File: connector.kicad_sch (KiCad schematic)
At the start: 4 parts, among them J1 Screw_Terminal_01x04

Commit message: ongoing add of MCU, etc.
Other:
- title: multiplex I2C to 6P4C connectors -> Multiplex I2C to Screw Terminal connectors
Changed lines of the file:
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@@
 	(paper "A4")
 	(title_block
-		(title "multiplex I2C to 6P4C connectors")
-		(date "2024-07-25")
-		(rev "v0.1.0")
+		(title "Multiplex I2C to Screw Terminal connectors")
+		(date "2025-09-07")
+		(rev "v0.2.0")
 	)
 	(junction

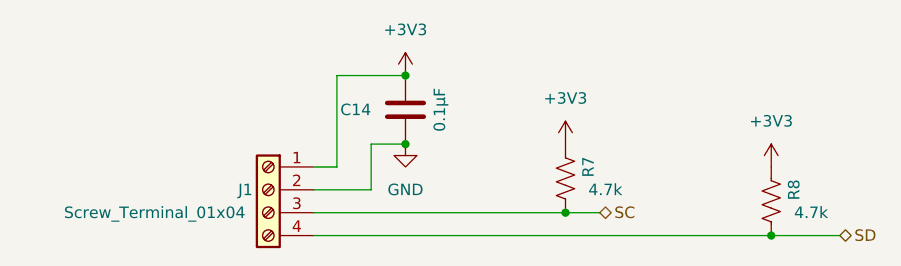
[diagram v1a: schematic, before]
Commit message: symbols an footprints added for f411 change. ERC passes.
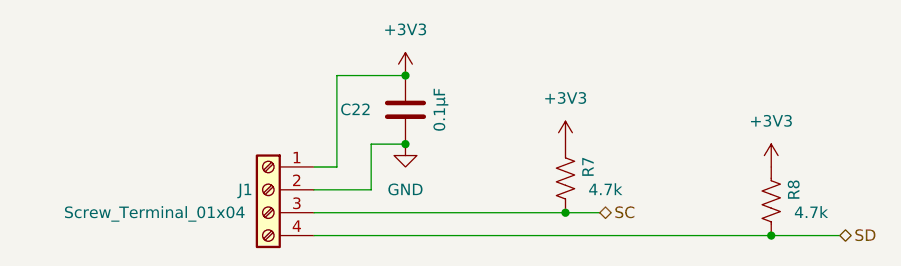
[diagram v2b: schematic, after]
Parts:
- renumbered C14 to C22
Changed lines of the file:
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@@
 			(project "multiplexI2CwithRJ11"
 				(path "/0c2d0c14-8850-4a30-bb78-b2f40cb442ba/0e7b750d-8e4e-450e-948f-cf92910adbb7"
-					(reference "#PWR051")
+					(reference "#PWR016")
 					(unit 1)
 				)
 				(path "/0c2d0c14-8850-4a30-bb78-b2f40cb442ba/24b4e8ef-9825-49f5-9404-579a6ea7b19b"
-					(reference "#PWR059")
+					(reference "#PWR025")
 					(unit 1)
 				)
 				(path "/0c2d0c14-8850-4a30-bb78-b2f40cb442ba/28f5dbbe-14b4-4c25-86a6-457951a84750"
-					(reference "#PWR071")
+					(reference "#PWR040")
 					(unit 1)
 				)
 				(path "/0c2d0c14-8850-4a30-bb78-b2f40cb442ba/4d3cd71d-38ce-404a-8590-119e12741a1e"
-					(reference "#PWR055")
+					(reference "#PWR021")
 					(unit 1)
 				)
 				(path "/0c2d0c14-8850-4a30-bb78-b2f40cb442ba/8a12c970-6e82-4f99-ab8e-e5d673f5e8d9"
-					(reference "#PWR045")
+					(reference "#PWR012")
 					(unit 1)
 				)
 				(path "/0c2d0c14-8850-4a30-bb78-b2f40cb442ba/96274ab6-b7f5-49e6-b2bc-a2b6a3cb42d1"
-					(reference "#PWR067")
+					(reference "#PWR033")
 					(unit 1)
 				)
@@
 				)
 				(path "/0c2d0c14-8850-4a30-bb78-b2f40cb442ba/f2b2a76e-3be2-4491-ad7e-06b9b1e9bf9c"
-					(reference "#PWR063")
+					(reference "#PWR029")
 					(unit 1)
 				)
@@
 			(project "multiplexI2CwithRJ11"
 				(path "/0c2d0c14-8850-4a30-bb78-b2f40cb442ba/0e7b750d-8e4e-450e-948f-cf92910adbb7"
-					(reference "#PWR047")
+					(reference "#PWR015")
 					(unit 1)
 				)
 				(path "/0c2d0c14-8850-4a30-bb78-b2f40cb442ba/24b4e8ef-9825-49f5-9404-579a6ea7b19b"
-					(reference "#PWR057")
+					(reference "#PWR024")
 					(unit 1)
 				)
 				(path "/0c2d0c14-8850-4a30-bb78-b2f40cb442ba/28f5dbbe-14b4-4c25-86a6-457951a84750"
-					(reference "#PWR069")
+					(reference "#PWR036")
 					(unit 1)
 				)
 				(path "/0c2d0c14-8850-4a30-bb78-b2f40cb442ba/4d3cd71d-38ce-404a-8590-119e12741a1e"
-					(reference "#PWR053")
+					(reference "#PWR019")
 					(unit 1)
 				)
 				(path "/0c2d0c14-8850-4a30-bb78-b2f40cb442ba/8a12c970-6e82-4f99-ab8e-e5d673f5e8d9"
-					(reference "#PWR040")
+					(reference "#PWR011")
 					(unit 1)
 				)
 				(path "/0c2d0c14-8850-4a30-bb78-b2f40cb442ba/96274ab6-b7f5-49e6-b2bc-a2b6a3cb42d1"
-					(reference "#PWR065")
+					(reference "#PWR032")
 					(unit 1)
 				)
@@
 				)
 				(path "/0c2d0c14-8850-4a30-bb78-b2f40cb442ba/f2b2a76e-3be2-4491-ad7e-06b9b1e9bf9c"
-					(reference "#PWR061")
+					(reference "#PWR028")
 					(unit 1)
 				)
@@
 		(on_board yes)
 		(dnp no)
-		(property "Reference" "C14"
+		(property "Reference" "C22"
 			(at 81.28 35.56 0)
 			(effects
@@
 			(project "multiplexI2CwithRJ11"
 				(path "/0c2d0c14-8850-4a30-bb78-b2f40cb442ba/0e7b750d-8e4e-450e-948f-cf92910adbb7"
-					(reference "C16")
+					(reference "C3")
 					(unit 1)
 				)
@@
 				)
 				(path "/0c2d0c14-8850-4a30-bb78-b2f40cb442ba/4d3cd71d-38ce-404a-8590-119e12741a1e"
-					(reference "C17")
+					(reference "C4")
 					(unit 1)
 				)
 				(path "/0c2d0c14-8850-4a30-bb78-b2f40cb442ba/8a12c970-6e82-4f99-ab8e-e5d673f5e8d9"
-					(reference "C15")
+					(reference "C2")
 					(unit 1)
 				)
@@
 				)
 				(path "/0c2d0c14-8850-4a30-bb78-b2f40cb442ba/e657843b-000b-4d7c-a001-36698309a032"
-					(reference "C14")
+					(reference "C22")
 					(unit 1)
 				)
@@
 			)
 		)
-		(property "Description" "Generic screw terminal, single row, 01x04"
+		(property "Description" "Generic screw terminal, single row, 01x04, script generated (kicad-library-utils/schlib/autogen/connector/)"
 			(at 69.85 44.45 0)
 			(effects
@@
 			(project "multiplexI2CwithRJ11"
 				(path "/0c2d0c14-8850-4a30-bb78-b2f40cb442ba/0e7b750d-8e4e-450e-948f-cf92910adbb7"
-					(reference "#PWR052")
+					(reference "#PWR017")
 					(unit 1)
 				)
 				(path "/0c2d0c14-8850-4a30-bb78-b2f40cb442ba/24b4e8ef-9825-49f5-9404-579a6ea7b19b"
-					(reference "#PWR060")
+					(reference "#PWR026")
 					(unit 1)
 				)
 				(path "/0c2d0c14-8850-4a30-bb78-b2f40cb442ba/28f5dbbe-14b4-4c25-86a6-457951a84750"
-					(reference "#PWR072")
+					(reference "#PWR043")
 					(unit 1)
 				)
 				(path "/0c2d0c14-8850-4a30-bb78-b2f40cb442ba/4d3cd71d-38ce-404a-8590-119e12741a1e"
-					(reference "#PWR056")
+					(reference "#PWR022")
 					(unit 1)
 				)
 				(path "/0c2d0c14-8850-4a30-bb78-b2f40cb442ba/8a12c970-6e82-4f99-ab8e-e5d673f5e8d9"
-					(reference "#PWR046")
+					(reference "#PWR013")
 					(unit 1)
 				)
 				(path "/0c2d0c14-8850-4a30-bb78-b2f40cb442ba/96274ab6-b7f5-49e6-b2bc-a2b6a3cb42d1"
-					(reference "#PWR068")
+					(reference "#PWR034")
 					(unit 1)
 				)
@@
 				)
 				(path "/0c2d0c14-8850-4a30-bb78-b2f40cb442ba/f2b2a76e-3be2-4491-ad7e-06b9b1e9bf9c"
-					(reference "#PWR064")
+					(reference "#PWR030")
 					(unit 1)
 				)
@@
 			(project "multiplexI2CwithRJ11"
 				(path "/0c2d0c14-8850-4a30-bb78-b2f40cb442ba/0e7b750d-8e4e-450e-948f-cf92910adbb7"
-					(reference "#PWR048")
+					(reference "#PWR014")
 					(unit 1)
 				)
 				(path "/0c2d0c14-8850-4a30-bb78-b2f40cb442ba/24b4e8ef-9825-49f5-9404-579a6ea7b19b"
-					(reference "#PWR058")
+					(reference "#PWR023")
 					(unit 1)
 				)
 				(path "/0c2d0c14-8850-4a30-bb78-b2f40cb442ba/28f5dbbe-14b4-4c25-86a6-457951a84750"
-					(reference "#PWR070")
+					(reference "#PWR035")
 					(unit 1)
 				)
 				(path "/0c2d0c14-8850-4a30-bb78-b2f40cb442ba/4d3cd71d-38ce-404a-8590-119e12741a1e"
-					(reference "#PWR054")
+					(reference "#PWR018")
 					(unit 1)
 				)
 				(path "/0c2d0c14-8850-4a30-bb78-b2f40cb442ba/8a12c970-6e82-4f99-ab8e-e5d673f5e8d9"
-					(reference "#PWR043")
+					(reference "#PWR010")
 					(unit 1)
 				)
 				(path "/0c2d0c14-8850-4a30-bb78-b2f40cb442ba/96274ab6-b7f5-49e6-b2bc-a2b6a3cb42d1"
-					(reference "#PWR066")
+					(reference "#PWR031")
 					(unit 1)
 				)
@@
 				)
 				(path "/0c2d0c14-8850-4a30-bb78-b2f40cb442ba/f2b2a76e-3be2-4491-ad7e-06b9b1e9bf9c"
-					(reference "#PWR062")
-					(unit 1)
-				)
+					(reference "#PWR027")
+					(unit 1)
+				)

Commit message: ongoing
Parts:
- C22: footprint ProjectLib:C_0805_2012Metric -> ProjectLib:C_0402_1005Metric
- R7, R8: footprint ProjectLib:R_0603_1608Metric -> ProjectLib:R_0402_1005Metric
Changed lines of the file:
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@@
 			)
 		)
-		(property "Footprint" "ProjectLib:R_0603_1608Metric"
+		(property "Footprint" "ProjectLib:R_0402_1005Metric"
 			(at 103.886 43.434 90)
 			(effects
@@
 			)
 		)
-		(property "Footprint" "ProjectLib:R_0603_1608Metric"
+		(property "Footprint" "ProjectLib:R_0402_1005Metric"
 			(at 126.746 45.974 90)
 			(effects
@@
 			)
 		)
-		(property "Footprint" "ProjectLib:C_0805_2012Metric"
+		(property "Footprint" "ProjectLib:C_0402_1005Metric"
 			(at 84.1248 39.37 0)
 			(effects

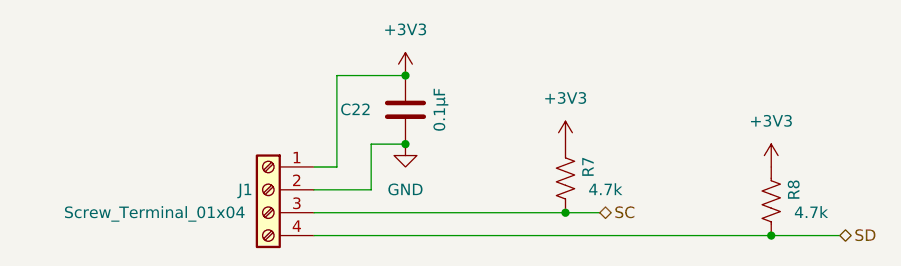
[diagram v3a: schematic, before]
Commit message: adding MCU, ongoing.
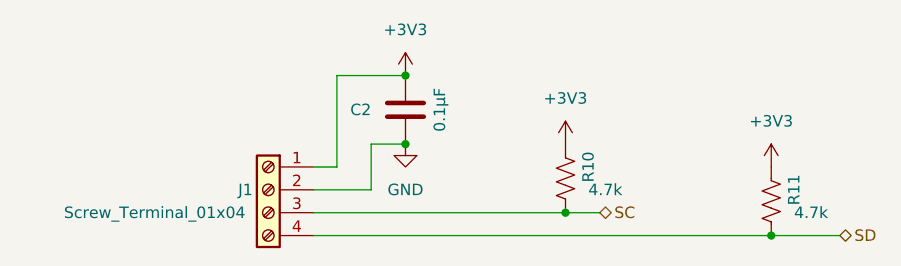
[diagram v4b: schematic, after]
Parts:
- renumbered C22 to C2, R7 to R10, R8 to R11
